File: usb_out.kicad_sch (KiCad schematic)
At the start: 5 parts

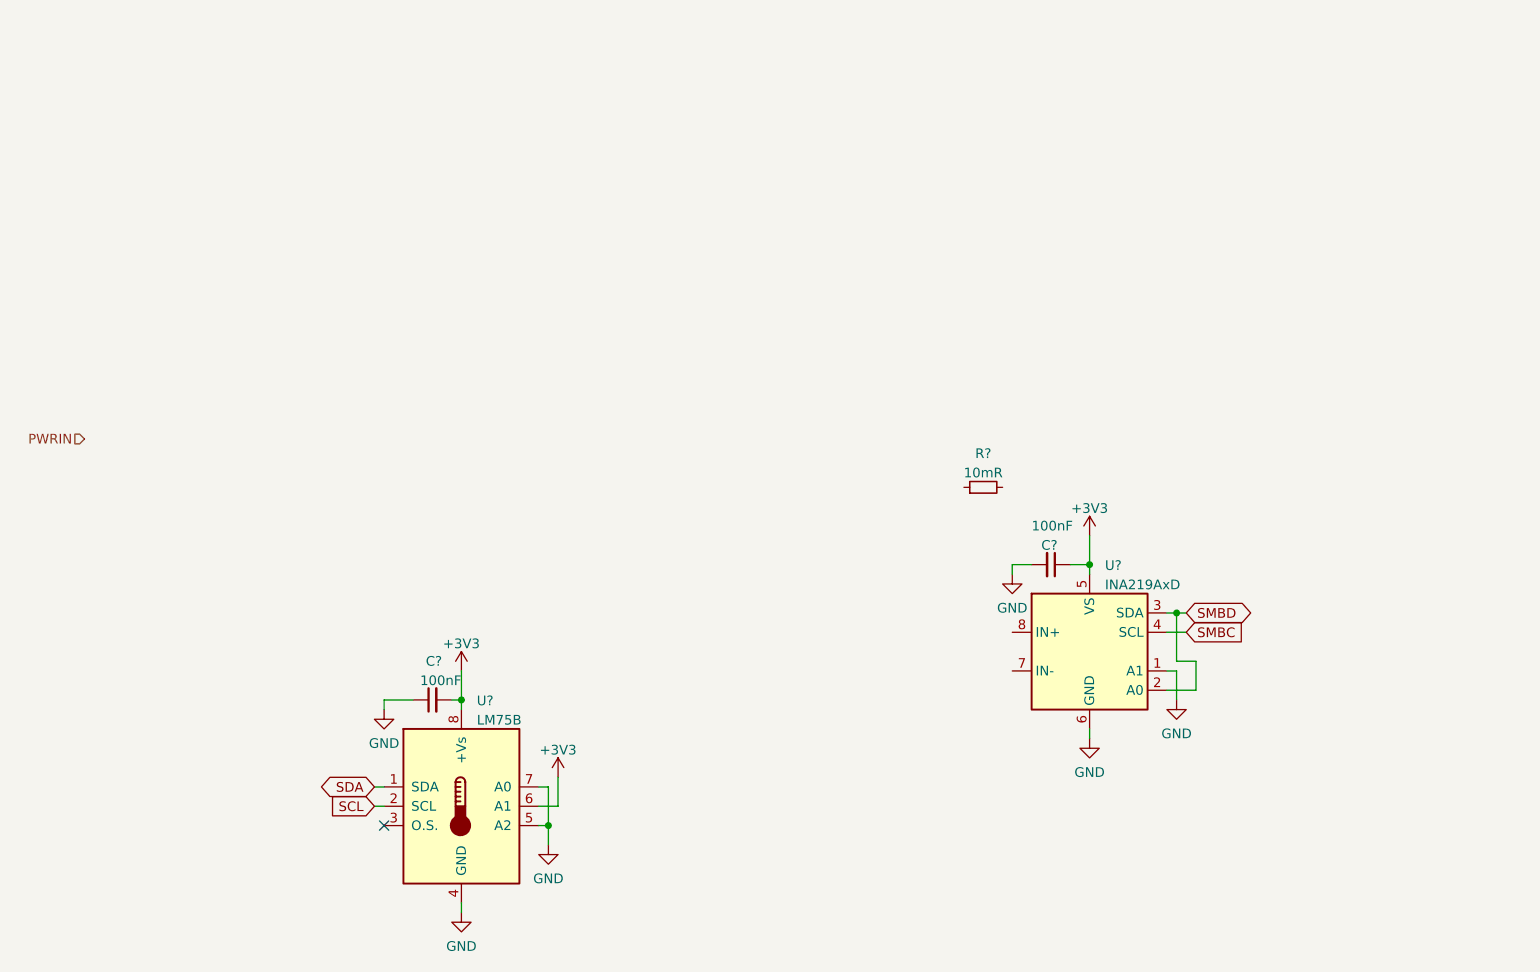
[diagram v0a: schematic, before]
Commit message: Add partial DC output circuitry
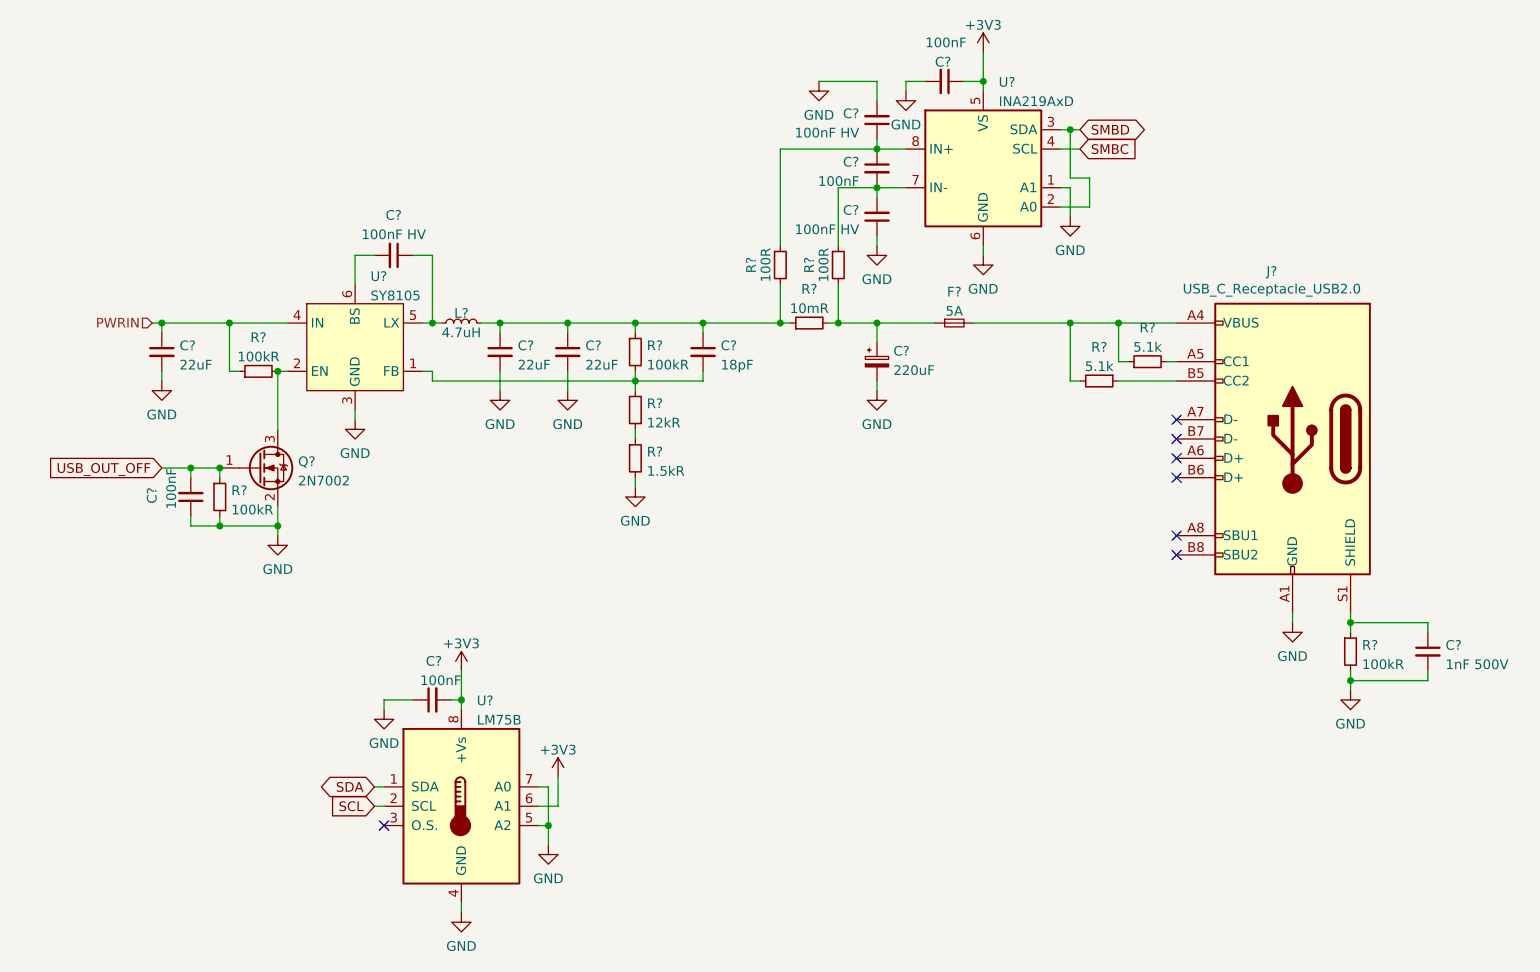
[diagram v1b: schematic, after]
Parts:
- removed R?: 10mR, Resistor_SMD:R_0805_2012Metric, symbol Device:R_Small
- added C?: 18pF, Capacitor_SMD:C_0402_1005Metric, symbol Device:C_Small
- added C? (x3): 100nF HV, Capacitor_SMD:C_0603_1608Metric, symbol Device:C_Small
- added C? (x2): 100nF, Capacitor_SMD:C_0402_1005Metric, symbol Device:C_Small
- added C? (x3): 22uF, Capacitor_SMD:C_0805_2012Metric, symbol Device:C_Small
- added C?: 1nF 500V, Capacitor_SMD:C_1206_3216Metric, symbol Device:C_Small
- added C?: 220uF, Capacitor_SMD:CP_Elec_6.3x5.4, symbol Device:C_Polarized_Small
- added F?: 5A, Fuse:Fuse_1206_3216Metric, symbol Device:Fuse_Small
- added J?: USB_C_Receptacle_USB2.0, Connector_USB:USB_C_Receptacle_Palconn_UTC16-G, symbol Connector:USB_C_Receptacle_USB2.0
- added L?: 4.7uH, Inductor_SMD:L_Bourns_SRP7028A_7.3x6.6mm, symbol Device:L_Small
- added Q?: 2N7002, Package_TO_SOT_SMD:SOT-23, symbol Transistor_FET:2N7002
- added R? (x3): 100kR, Resistor_SMD:R_0402_1005Metric, symbol Device:R_Small
- added R? (x2): 100R, Resistor_SMD:R_0402_1005Metric, symbol Device:R_Small
- added R?: 100kR, Resistor_SMD:R_1206_3216Metric, symbol Device:R_Small
- added R?: 12kR, Resistor_SMD:R_0402_1005Metric, symbol Device:R_Small
- added R? (x2): 5.1k, Resistor_SMD:R_0402_1005Metric, symbol Device:R_Small
- added R?: 10mR, Resistor_SMD:R_0805_2012Metric, symbol Device:R_Small
- added R?: 1.5kR, Resistor_SMD:R_0402_1005Metric, symbol Device:R_Small
- added U?: SY8105, Package_TO_SOT_SMD:TSOT-23-6, symbol Regulator_Switching_Silergy:SY8105
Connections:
- net GND: now also C?.1, C?.1, C?.2, C?.2, C?.2, C?.2, C?.2, C?.2, J?.A1 (GND), J?.A12 (GND), J?.B1 (GND), J?.B12 (GND), Q?.2 (S), R?.2, R?.2, R?.2, U?.3 (GND)
- net PWRIN: now also C?.1, R?.1, U?.4 (IN)
- net at U?.7 (IN-): now also C?.2, C?.2, R?.1
- net at U?.8 (IN+): now also C?.1, C?.1, R?.1
- new net: Q?.3 (D), R?.2, U?.2 (EN)
- new net: C?.1, F?.1, R?.2, R?.2
- new net: F?.2, J?.A4 (VBUS), J?.A9 (VBUS), J?.B4 (VBUS), J?.B9 (VBUS), R?.1, R?.2
- new net: C?.1, C?.1, C?.1, L?.2, R?.1, R?.1, R?.2
- new net: C?.2, R?.2, R?.2, U?.1 (FB)
- new net: C?.1, L?.1, U?.5 (LX)
- new net: C?.2, U?.6 (BS)
- new net: C?.1, J?.S1 (SHIELD), R?.1
- new net: R?.1, R?.1
- new net: J?.B5 (CC2), R?.1
- new net: J?.A5 (CC1), R?.2
- new net USB_OUT_OFF: C?.2, Q?.1 (G), R?.1
- no-connect marks 1 -> 7
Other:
- moved on the sheet: C?, U?

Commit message: Finish DC output schematic capture
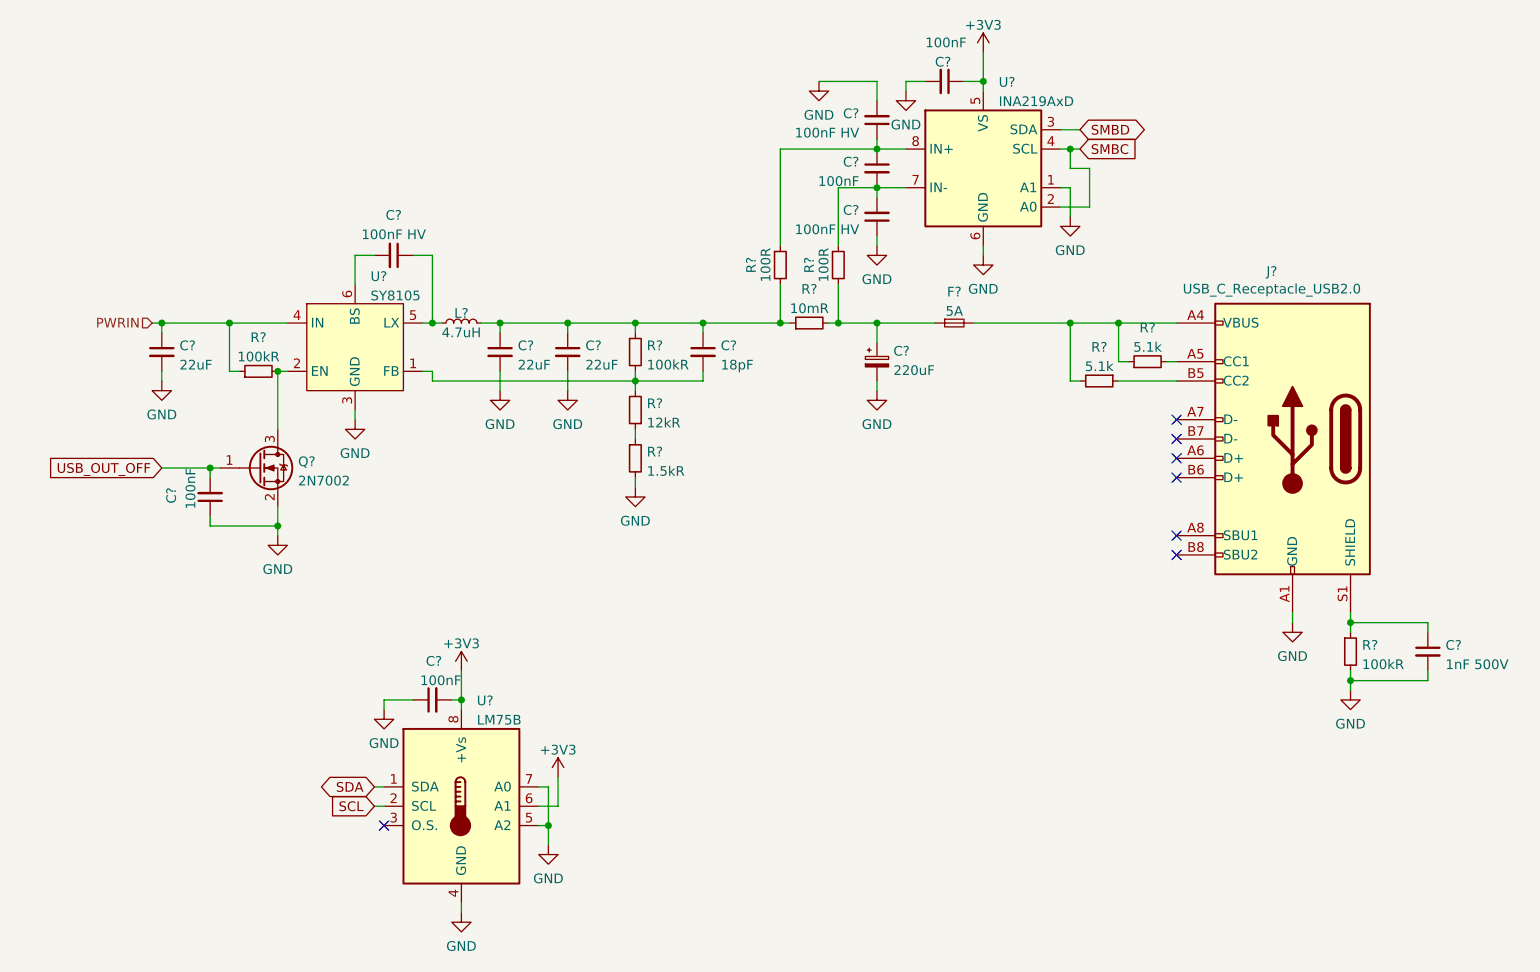
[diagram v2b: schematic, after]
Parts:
- removed R?: 100kR, Resistor_SMD:R_0402_1005Metric, symbol Device:R_Small
- removed U?: INA219AxD, Package_SO:SOIC-8_3.9x4.9mm_P1.27mm, symbol Analog_ADC:INA219AxD
- added U?: INA219AxD, Package_SO:SOIC-8_3.9x4.9mm_P1.27mm, symbol Analog_ADC:INA219AxD
- C?: footprint Capacitor_SMD:CP_Elec_6.3x5.4 -> Capacitor_SMD:CP_Elec_6.3x7.7; LCSC C72494 -> C340768
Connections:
- net +3V3: now also U?.5 (VS)
- net GND: now also U?.1 (A1), U?.6 (GND)
- net SMBC: now also U?.2 (A0), U?.4 (SCL)
- net SMBD: now also U?.3 (SDA)
- net at C?.2, C?.2, R?.1: now also U?.7 (IN-)
- net at C?.1, C?.1, R?.1: now also U?.8 (IN+)
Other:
- moved on the sheet: C?

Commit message: Add barrel jack footprints
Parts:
- U?: footprint (none) -> Package_SO:MSOP-8_3x3mm_P0.65mm; LCSC (none) -> C2837470
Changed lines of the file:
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@@
       (effects (font (size 1.27 1.27)) (justify left))
     )
-    (property "Footprint" "" (id 2) (at 92.71 129.54 0)
+    (property "Footprint" "Package_SO:MSOP-8_3x3mm_P0.65mm" (id 2) (at 92.71 129.54 0)
       (effects (font (size 1.27 1.27)) hide)
     )
@@
       (effects (font (size 1.27 1.27)) hide)
     )
+    (property "LCSC" "C2837470" (id 4) (at 92.71 129.54 0)
+      (effects (font (size 1.27 1.27)) hide)
+    )

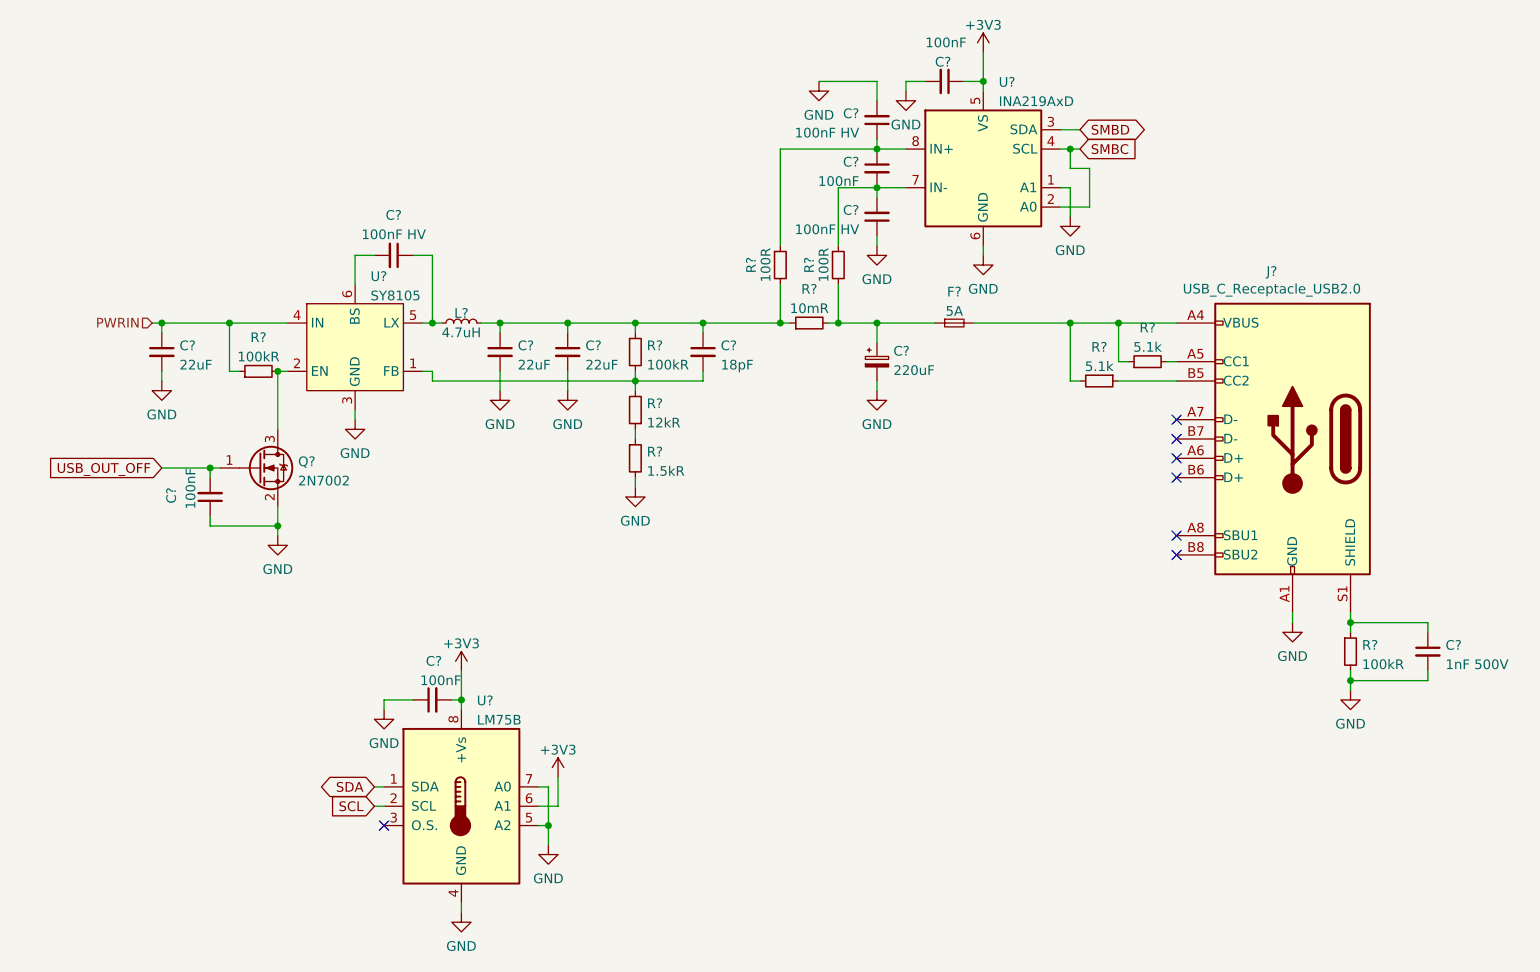
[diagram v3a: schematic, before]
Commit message: Add individually switchable outputs
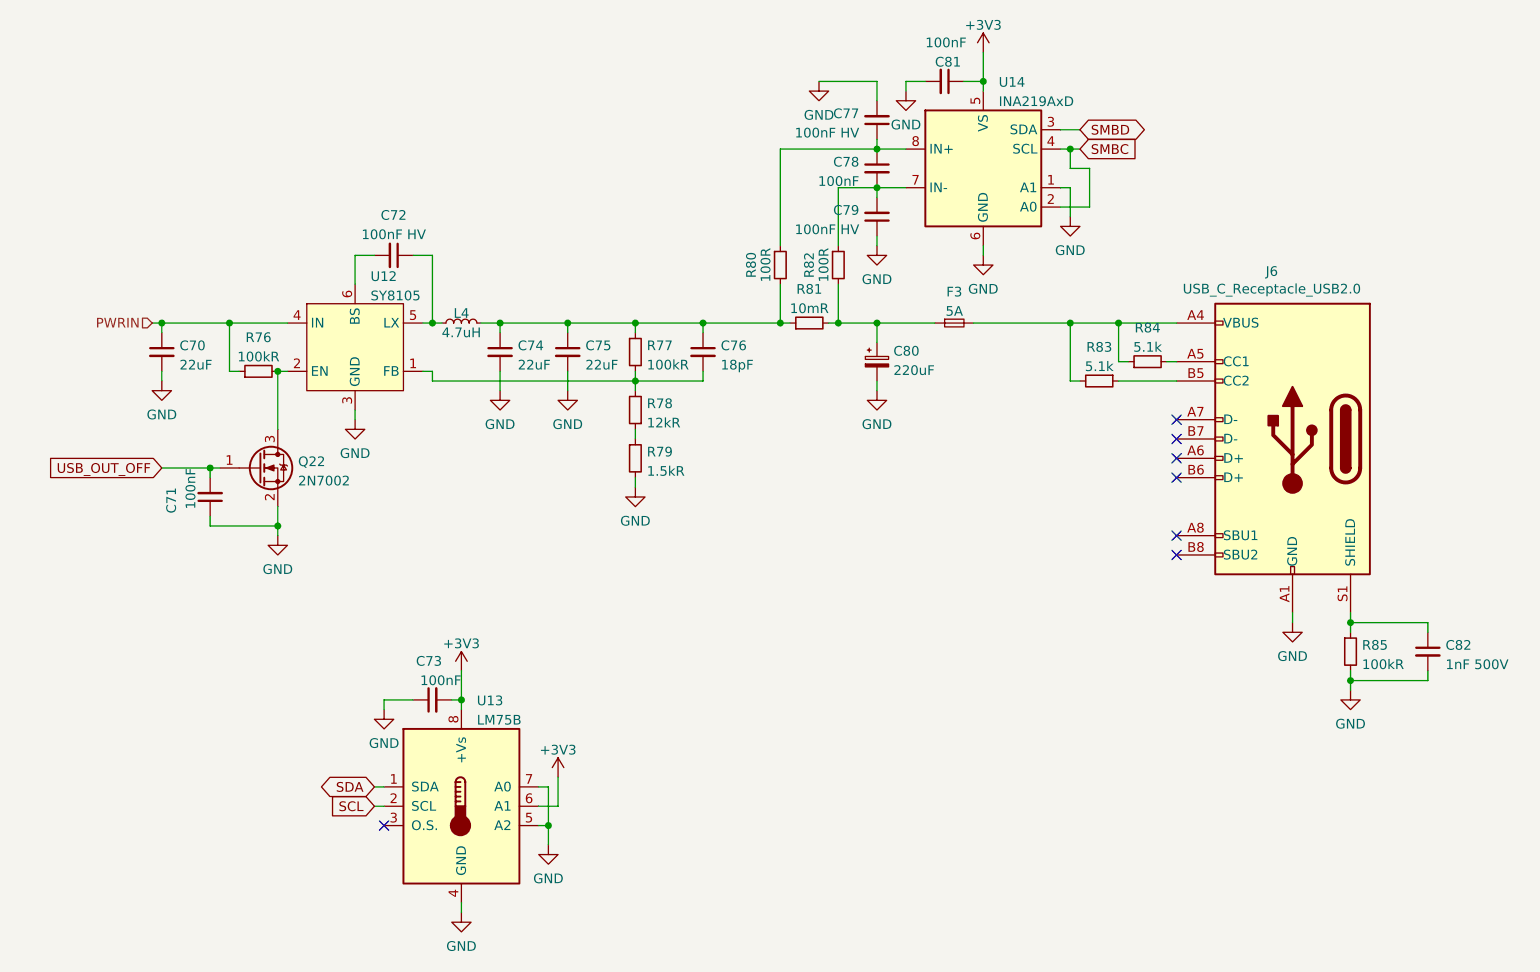
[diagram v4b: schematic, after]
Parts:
- gave numbers to parts that had none: 30
